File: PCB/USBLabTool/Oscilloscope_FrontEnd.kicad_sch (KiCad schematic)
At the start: 61 parts, among them J1 Chanel 1 input, J10 GPIO, J11 T_buf, J12 T_N5V, J13 ADC, J14 +3.3 V, J2 2174507-2, J3 T_att, J4 Conn_01x01, J5 T_acdc, J6 T_P5V, J7 T_amp, J8 T_pwm, J9 Conn_01x01, K1 G5V-2, Q1 IRLML6402TRPBF, U12 LMP7718, U2 AQY284SX, U3 CD74HC4316M96, U5 LTC1983ES6-5#TRPBF, U6 OPA863

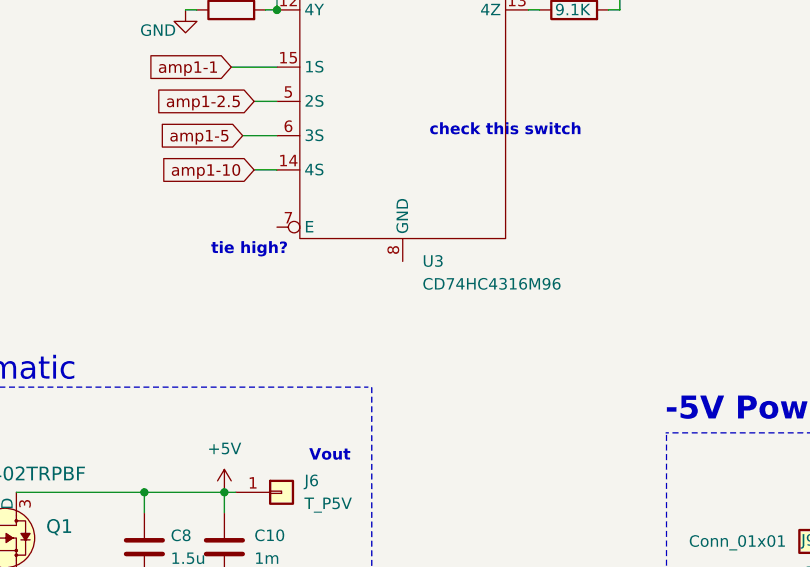
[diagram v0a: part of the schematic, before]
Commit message: added missing GND
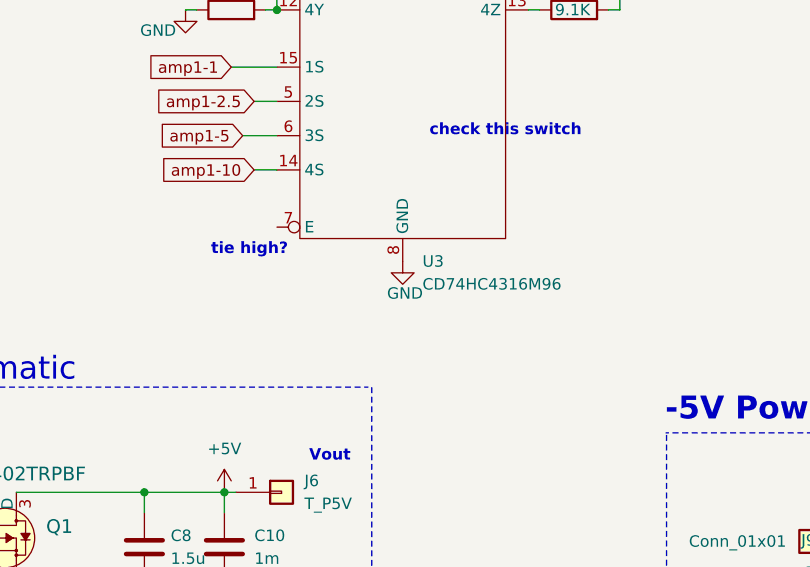
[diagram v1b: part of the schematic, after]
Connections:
- net GND: now also U3.8 (GND)
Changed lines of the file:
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@@
+	)
+	(symbol
+		(lib_id "power:GND")
+		(at 171.45 148.59 0)
+		(unit 1)
+		(exclude_from_sim no)
+		(in_bom yes)
+		(on_board yes)
+		(dnp no)
+		(property "Reference" "#PWR06"
+			(at 171.45 154.94 0)
+			(effects
+				(font
+					(size 1.27 1.27)
+				)
+				(hide yes)
+			)
+		)
+		(property "Value" "GND"
+			(at 171.704 152.146 0)
+			(effects
+				(font
+					(size 1.27 1.27)
+				)
+			)
+		)
+		(property "Footprint" ""
+			(at 171.45 148.59 0)
+			(effects
+				(font
+					(size 1.27 1.27)
+				)
+				(hide yes)
+			)
+		)
+		(property "Datasheet" ""
+			(at 171.45 148.59 0)
+			(effects
+				(font
+					(size 1.27 1.27)
+				)
+				(hide yes)
+			)
+		)
+		(property "Description" ""
+			(at 171.45 148.59 0)
+			(effects
+				(font
+					(size 1.27 1.27)
+				)
+				(hide yes)
+			)
+		)
+		(pin "1"
+		)
+		(instances
+			(project "USBLabTool"
+				(path "/b5440f7d-90d5-417e-adc2-aa6b11e5424d/4269701b-4537-45be-98a2-a1633b405066"
+					(reference "#PWR06")
+					(unit 1)
+				)
+			)
+		)
 	)
 	(symbol

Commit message: Starting PCB layout
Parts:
- removed J10: GPIO, Connector_PinHeader_2.54mm:PinHeader_1x10_P2.54mm_Vertical, symbol Connector_Generic:Conn_01x10
- removed J2: 2174507-2, J_SMD_2174507-2-5_7.8_5_2.71, symbol 2174507-2:2174507-2
- removed Q1: IRLML6402TRPBF, digikey-footprints:SOT-23-3, symbol dk_Transistors-FETs-MOSFETs-Single:IRLML6402TRPBF
- removed U12: LMP7718, Package_SO:VSSOP-8_3x3mm_P0.65mm, symbol USBLabTool:LMP7718MM/NOPB
- removed U3: CD74HC4316M96, symbol USBLabTool:CD74HC4316M96
- removed U5: LTC1983ES6-5#TRPBF, Package_TO_SOT_SMD:SOT-23-6_Handsoldering, symbol LTC1983ES6-5_TRPBF:LTC1983ES6-5#TRPBF
- added C11, C12, C16, C24, C26, c23: 100n, Capacitor_SMD:C_0603_1608Metric_Pad1.08x0.95mm_HandSolder, symbol Device:C
- added C11: 47n, Capacitor_SMD:C_0603_1608Metric_Pad1.08x0.95mm_HandSolder, symbol Device:C
- added C25: 160p, Capacitor_SMD:C_0603_1608Metric_Pad1.08x0.95mm_HandSolder, symbol Device:C
- added C5: 200p, Capacitor_SMD:C_0603_1608Metric_Pad1.08x0.95mm_HandSolder, symbol Device:C
- added D3: 1N4148, Diode_THT:D_DO-35_SOD27_P7.62mm_Horizontal, symbol Diode:1N4148
- added D4: BAV199DW, Package_TO_SOT_SMD:SOT-23, symbol Diode:BAV199DW
- added GD2: GDT_SH90, footprints:GDT_SH_LTF, symbol Device:GDT_2Pin
- added J10: T_pwm, Connector_PinHeader_2.54mm:PinHeader_1x01_P2.54mm_Vertical, symbol Connector_Generic:Conn_01x01
- added J15: ADC2, Connector_PinHeader_2.54mm:PinHeader_1x01_P2.54mm_Vertical, symbol Connector_Generic:Conn_01x01
- added J16: +3.3 V, Connector_PinHeader_2.54mm:PinHeader_1x01_P2.54mm_Vertical, symbol Connector_Generic:Conn_01x01
- added J2: Chanel 1 input, Connector_PinHeader_2.54mm:PinHeader_1x01_P2.54mm_Vertical, symbol Connector_Generic:Conn_01x01
- added K2: G5V-2, Relay_THT:Relay_DPDT_Omron_G5V-2, symbol Relay:G5V-2
- added L2: 10u, Inductor_SMD:L_0603_1608Metric_Pad1.05x0.95mm_HandSolder, symbol pspice:INDUCTOR
- added R18: 68K, Resistor_SMD:R_0603_1608Metric_Pad0.98x0.95mm_HandSolder, symbol Device:R
- added R19: 820K, Resistor_SMD:R_0603_1608Metric_Pad0.98x0.95mm_HandSolder, symbol Device:R
- added R20: 200k, Resistor_SMD:R_0603_1608Metric_Pad0.98x0.95mm_HandSolder, symbol Device:R
- added R21: 240, Resistor_SMD:R_0603_1608Metric_Pad0.98x0.95mm_HandSolder, symbol Device:R
- added R22, R27, R31: 1K, Resistor_SMD:R_0603_1608Metric_Pad0.98x0.95mm_HandSolder, symbol Device:R
- added R23, R28: 6.2, Resistor_SMD:R_0603_1608Metric_Pad0.98x0.95mm_HandSolder, symbol Device:R
- added R24: 1.5K, Resistor_SMD:R_0603_1608Metric_Pad0.98x0.95mm_HandSolder, symbol Device:R
- added R25: 3.9K, Resistor_SMD:R_0603_1608Metric_Pad0.98x0.95mm_HandSolder, symbol Device:R
- added R26: 9.1K, Resistor_SMD:R_0603_1608Metric_Pad0.98x0.95mm_HandSolder, symbol Device:R
- added R29, R30: 2K, Resistor_SMD:R_0603_1608Metric_Pad0.98x0.95mm_HandSolder, symbol Device:R
- added R32: 100, Resistor_SMD:R_0603_1608Metric_Pad0.98x0.95mm_HandSolder, symbol Device:R
- added U1: AQY284SX, Package_SO:SOP-4_3.8x4.1mm_P2.54mm, symbol Relay_SolidState:TLP3123
- added U3 (x2): CD74HC4316M96, Package_SO:SOIC-16_3.9x9.9mm_P1.27mm, symbol USBLabTool:CD74HC4316M96
- added U5, U8: LMP7718, Package_SO:VSSOP-8_3x3mm_P0.65mm, symbol USBLabTool:LMP7718MM/NOPB
- added U7: OPA863, Package_TO_SOT_SMD:SOT-23-6_Handsoldering, symbol Amplifier_Operational:ADA4807-1
- C10: value 1m -> 820p
- C14: value 10u -> 100n
- C15: value 1u -> 100n
- C20: value 10u -> 1u
- C6: value 10u -> 820p
- C8: value 1.5u -> 68p
- GD2: renamed from GD1; footprint digikey-footprints:SH90_1 -> footprints:GDT_SH_LTF
- J12: value T_N5V -> T_buf
- J14: renamed from J13; value ADC -> ADC1
- J4: value Conn_01x01 -> T_att
- J6: value T_P5V -> T_acdc
- J9: value Conn_01x01 -> T_amp
- R6: value 27k -> 820K
- renumbered C7 to C10, C17 to C16, C9 to C17, C12 to C18, C13 to C20, C21 to C26, C22 to C28, C1 to C5, C2 to C6, C3 to C7, C4 to C8, D1 to D2, D2 to D4, J8 to J10, J11 to J12, J14 to J16, J3 to J4, J7 to J8, R5 to R10, R7 to R12, R9 to R17, R11 to R18, R10 to R19, R12 to R20, R13 to R23, R15 to R27, R14 to R29, R16 to R30, R17 to R32, R1 to R5, R2 to R6, R3 to R7, R4 to R8
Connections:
- net +3.3V: now also C26.1, D4.1 (A1), J16.1 (Pin_1)
- net +5V: now also C15.1, C16.1, U3.16 (V_CC), U3.16 (V_CC), U5.8 (V+), U7.5 (~{DISABLE}), U7.6 (V+), U8.8 (V+), c23.2; no longer C10.1, C14.1, C8.2, J6.1 (Pin_1), J9.1 (Pin_1)
- net -5V: now also C14.1, C11.1, C12.1, C24.1, U3.9 (V_EE), U3.9 (V_EE), U5.4 (V-), U7.2 (V-), U8.4 (V-); no longer C20.1, J12.1 (Pin_1)
- net GND: now also C15.2, C11.2, C12.2, C16.2, C24.2, C25.2, C26.2, C5.1, D3.2 (A), D4.2 (K2), GD2.2, K2.1, R18.1, R19.1, R22.1, R29.2, U1.2, U3.7 (E), U3.7 (E), U3.8 (GND), U3.8 (GND), c23.1; no longer C6.2, R6.2
- net acdc: now also R21.2
- net amp1-1: now also U3.15 (1S)
- net amp1-10: now also U3.14 (4S)
- net amp1-2.5: now also U3.5 (2S)
- net amp1-5: now also U3.6 (3S)
- net attenuate: now also D3.1 (K), K2.16
- net at C10.2, J5.1 (Pin_1), U2.3: now also U8.3 (+IN_A)
- net at C6.1: now also C5.2, K2.6, R19.2, R20.1; no longer J4.1 (Pin_1)
- net at J8.1 (Pin_1), R17.2, R18.2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: now also U8.1 (OUT_A)
- net at R17.1: now also U3.1 (1Z)
- net at R27.1, R30.1: now also U8.6 (-IN_B)
- net at R20.1: now also U3.13 (4Z)
- net at R23.2, R29.2: now also U8.5 (+IN_B)
- net at R12.2: now also U3.11 (3Y), U3.12 (4Y), U3.2 (1Y), U3.3 (2Y), U8.2 (-IN_A)
- net at R30.2, U6.3 (+): now also U8.7 (OUT_B)
- net at R6.1: now also C10.1, C8.2, K2.8, R18.2; no longer C8.1
- net at R19.1: now also U3.10 (3Z)
- net at R18.1: now also U3.4 (2Z)
- net ADC renamed ADC1
- net pwm renamed TIM2_CH1
- new net: C8.1, K2.9, R6.2
- new net: R23.1, U3.1 (1Z)
- new net: J9.1 (Pin_1), R23.2, R24.2, R25.2, R26.2, R27.1, U5.1 (OUT_A)
- new net: R25.1, U3.10 (3Z)
- new net: R29.1, R31.1, U5.6 (-IN_B)
- new net: R31.2, U5.7 (OUT_B), U7.3 (+)
- new net: J12.1 (Pin_1), R32.1, U7.1, U7.4 (-)
- new net: C20.1, J10.1 (Pin_1), L2.2, R30.1
- new net: R27.2, R30.2, U5.5 (+IN_B)
- new net: R24.1, U3.4 (2Z)
- new net: R22.2, U3.11 (3Y), U3.12 (4Y), U3.2 (1Y), U3.3 (2Y), U5.2 (-IN_A)
- new net: C6.2, K2.11, R20.2
- new net: C11.2, J6.1 (Pin_1), U1.3, U5.3 (+IN_A)
- new net: R21.1, U1.1
- new net: C11.1, J4.1 (Pin_1), K2.4, U1.4
- new net: GD2.1, J2.1 (Pin_1), K2.13
- new net: R26.1, U3.13 (4Z)
- new net: L2.1, R28.2
- new net ADC2: C25.1, D4.3 (K3A4), J15.1 (Pin_1), R32.2
- new net TIM2_CH2: R28.1
- new net amp2-1: U3.15 (1S)
- new net amp2-10: U3.14 (4S)
- new net amp2-2.5: U3.5 (2S)
- new net amp2-5: U3.6 (3S)
- no-connect marks 3 -> 0
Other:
- note added: "SCOPE CHAN 0"
- note added: "SCOPE CHAN 1"
- note added: "it's active low for the switch so ground the E"
- note removed: "-5V Power supply"
- note removed: "USB Soft Start Schematic"
- note removed: "Vout"
- note removed: "move these things to the Power_Supply sheet -5V might not be needed (awg already has it?) usb plug should be with MCU probably (psu part on power supply)"
- note removed: "need to change this to actual mcu pins"
- moved on the sheet: C10, C16, C17, C18, C20, C26, C28, C5, C6, C7, C8, D2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

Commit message: Finished PCB traces
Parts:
- J1: value Chanel 1 input -> Chanel 0 input
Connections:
- net acdc renamed CH0 ACDC
- net CH0 ACDC: no longer R21.2
- net attenuate renamed CH0_attenuate
- net CH0_attenuate: no longer D3.1 (K), K2.16
- new net CH1 ACDC: R21.2
- new net CH1_attenuate: D3.1 (K), K2.16
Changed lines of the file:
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@@
 		)
 	)
-	(text "tie high?"
-		(exclude_from_sim no)
-		(at 143.256 240.03 0)
-		(effects
-			(font
-				(size 1.27 1.27)
-				(thickness 0.254)
-				(bold yes)
-			)
-		)
-	)
 	(text "check this switch"
 		(exclude_from_sim no)
@@
 		)
 	)
-	(global_label "attenuate"
+	(global_label "CH1_attenuate"
 		(shape input)
 		(at 46.99 180.34 180)
@@
 		)
 		(property "Intersheetrefs" "${INTERSHEET_REFS}"
-			(at 35.6264 180.2606 0)
+			(at 30.2769 180.34 0)
 			(effects
 				(font
@@
 		)
 	)
-	(global_label "acdc"
+	(global_label "CH0 ACDC"
 		(shape input)
 		(at 119.38 73.66 180)
@@
 		)
 		(property "Intersheetrefs" "${INTERSHEET_REFS}"
-			(at 112.4917 73.5806 0)
+			(at 106.7186 73.66 0)
 			(effects
 				(font
@@
 		)
 	)
-	(global_label "acdc"
+	(global_label "CH1 ACDC"
 		(shape input)
 		(at 110.49 185.42 180)
@@
 		)
 		(property "Intersheetrefs" "${INTERSHEET_REFS}"
-			(at 103.6017 185.3406 0)
+			(at 97.8286 185.42 0)
 			(effects
 				(font
@@
 		)
 	)
-	(global_label "attenuate"
+	(global_label "CH0_attenuate"
 		(shape input)
 		(at 55.88 68.58 180)
@@
 		)
 		(property "Intersheetrefs" "${INTERSHEET_REFS}"
-			(at 44.5164 68.5006 0)
+			(at 39.1669 68.58 0)
 			(effects
 				(font
@@
 			)
 		)
-		(property "Value" "Chanel 1 input"
+		(property "Value" "Chanel 0 input"
 			(at 27.178 86.106 90)
 			(effects

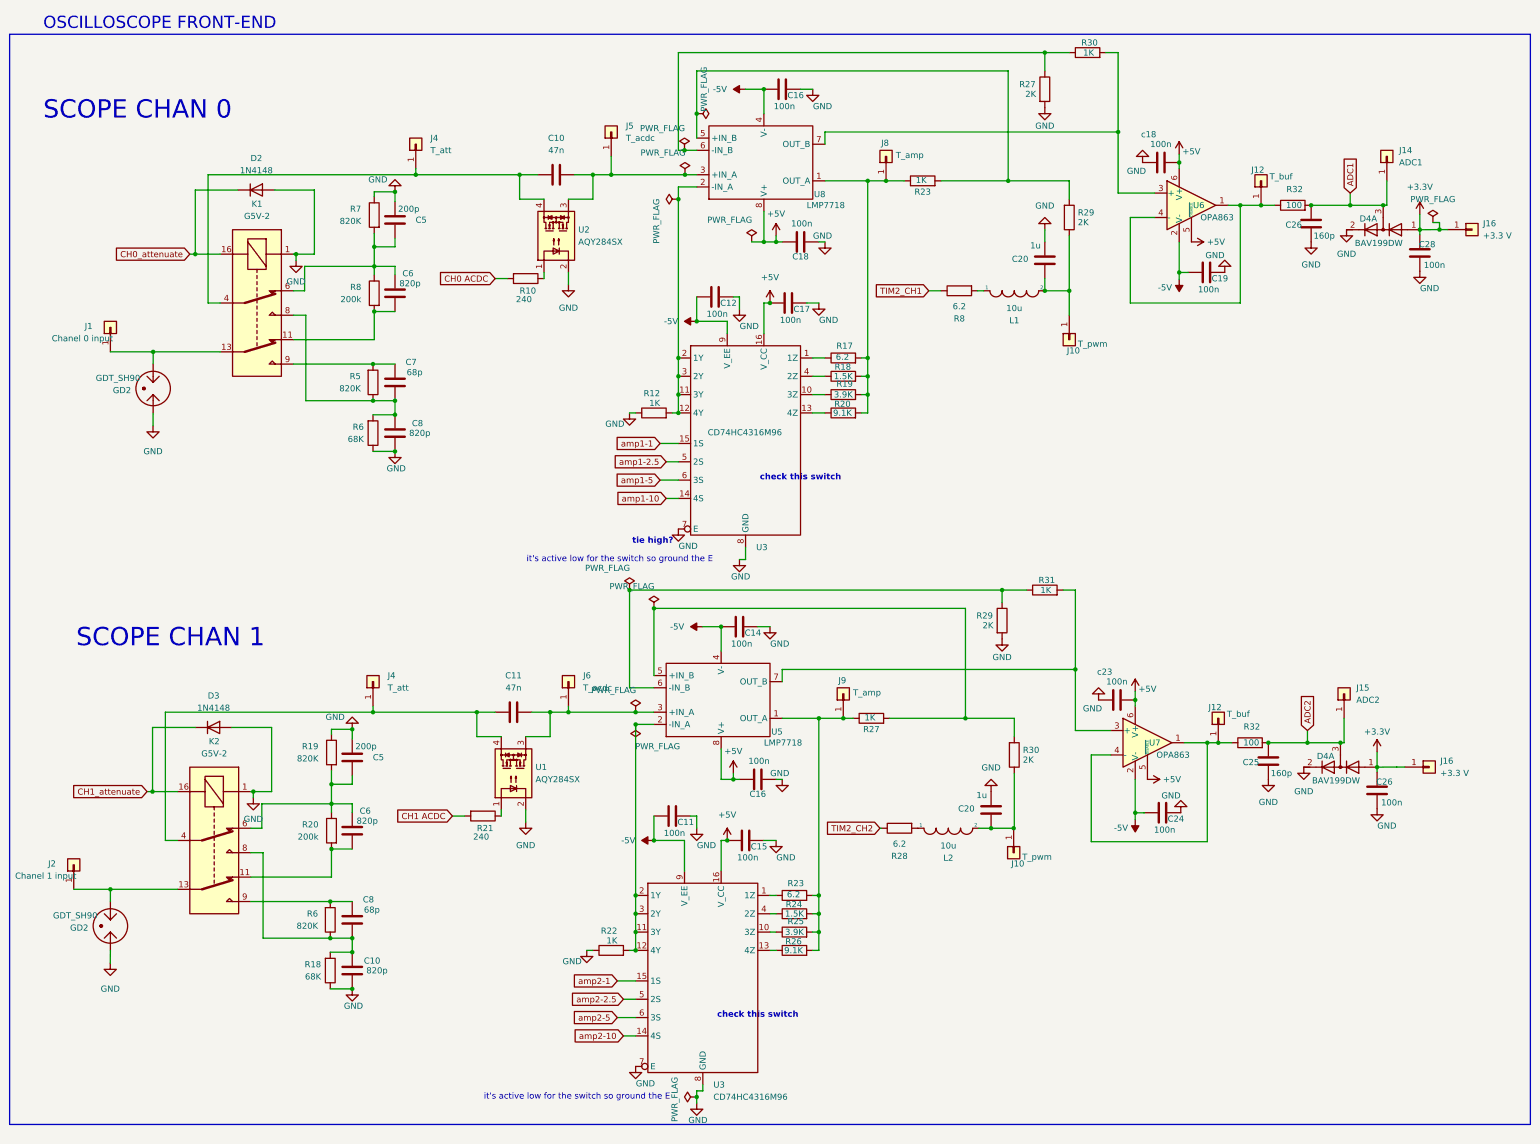
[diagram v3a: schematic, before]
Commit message: Moving files to where they should be
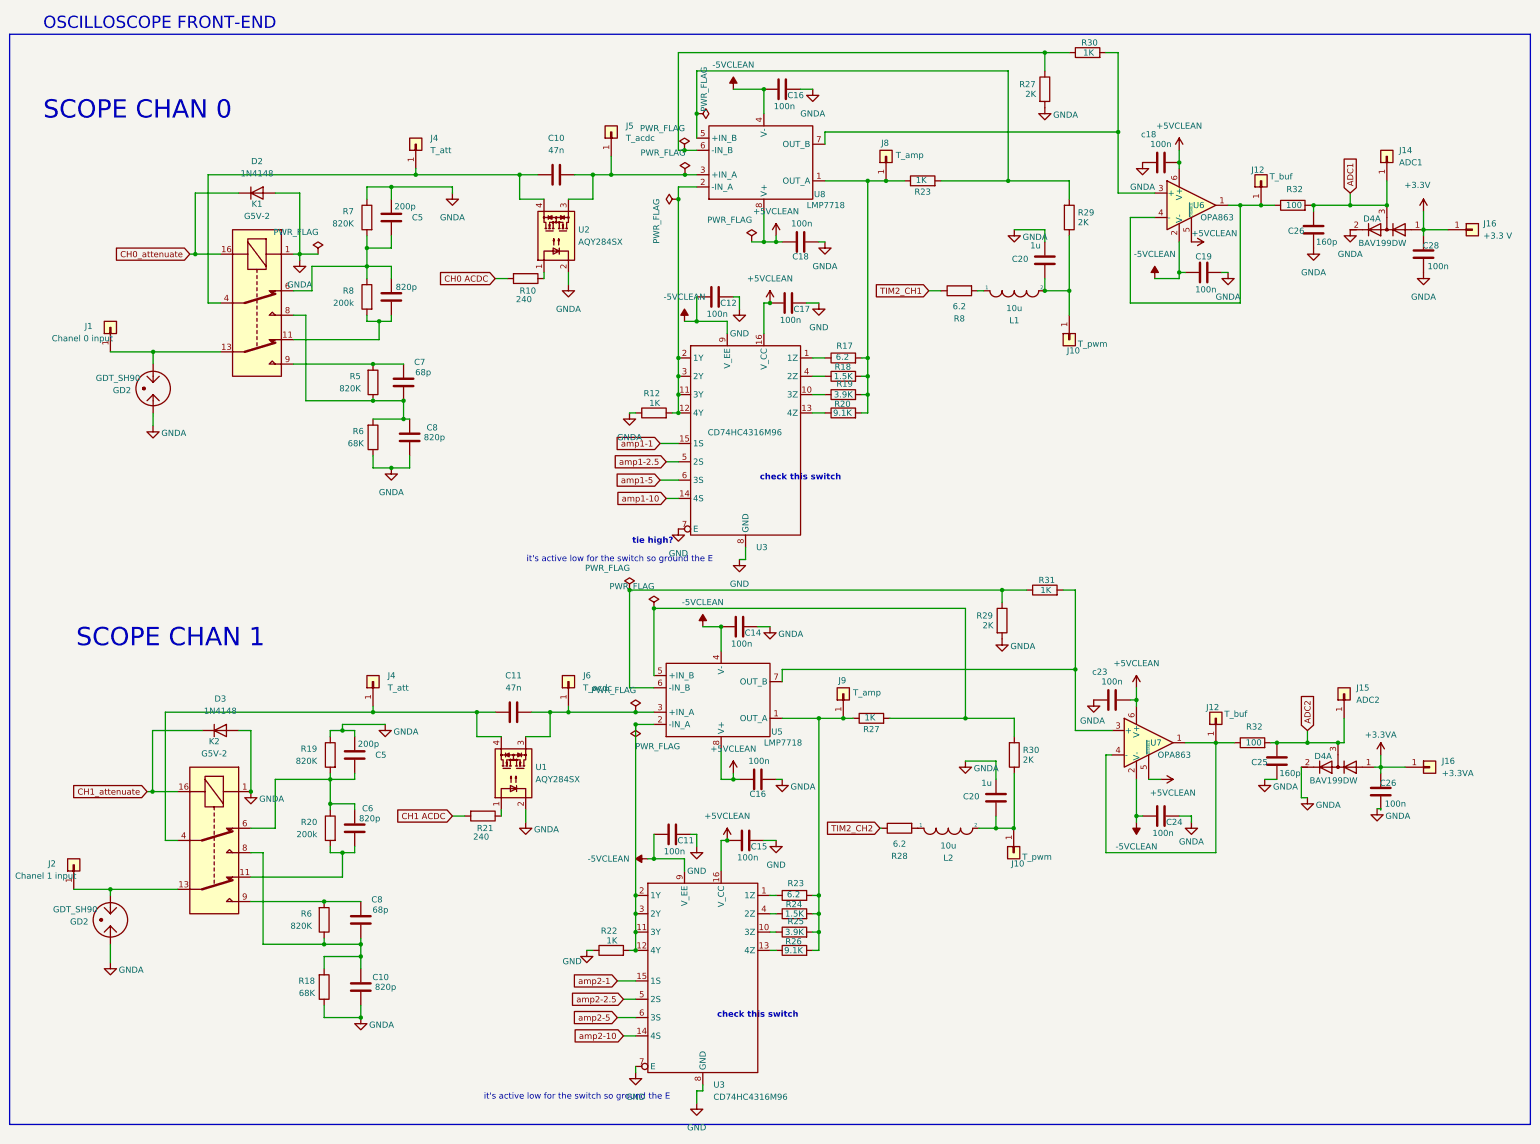
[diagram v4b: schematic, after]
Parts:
- J16: value +3.3 V -> +3.3VA
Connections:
- net +3.3V: no longer C26.1, D4.1 (A1), J16.1 (Pin_1)
- net GND: no longer C10.2, C14.2, C16.2, C16.2, C18.2, C19.2, C20.2, C20.2, C24.2, C25.2, C26.2, C26.2, C28.2, C5.1, C5.1, C8.2, D2.2 (A), D3.2 (A), D4.2 (K2), D4.2 (K2), GD2.2, GD2.2, K1.1, K2.1, R12.1, R18.1, R19.1, R27.2, R29.2, R6.1, R7.1, U1.2, U2.2, c18.1, c23.1
- net +5V renamed +5VCLEAN
- net -5V renamed -5VCLEAN
- new net +3.3VA: C26.1, D4.1 (A1), J16.1 (Pin_1)
- new net GNDA: C10.2, C14.2, C16.2, C16.2, C18.2, C19.2, C20.2, C20.2, C24.2, C25.2, C26.2, C26.2, C28.2, C5.1, C5.1, C8.2, D2.2 (A), D3.2 (A), D4.2 (K2), D4.2 (K2), GD2.2, GD2.2, K1.1, K2.1, R12.1, R18.1, R19.1, R27.2, R29.2, R6.1, R7.1, U1.2, U2.2, c18.1, c23.1
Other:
- moved on the sheet: C10, C11, C19, C20, C24, C25, C26, C28, C5, C6, C7, C8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

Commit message: Moving files to where they should be
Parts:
- D4: footprint Package_TO_SOT_SMD:SOT-23 -> Package_TO_SOT_SMD:SOT-363_SC-70-6_Handsoldering
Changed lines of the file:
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@@
 			)
 		)
-		(property "Footprint" "Package_TO_SOT_SMD:SOT-23"
+		(property "Footprint" "Package_TO_SOT_SMD:SOT-363_SC-70-6_Handsoldering"
 			(at 292.1 63.5 0)
 			(effects
@@
 			)
 		)
+		(property "Purpose" ""
+			(at 304.8 63.5 0)
+			(effects
+				(font
+					(size 1.27 1.27)
+				)
+				(hide yes)
+			)
+		)
 		(pin "1"
 		)
@@
 			)
 		)
-		(property "Footprint" "Package_TO_SOT_SMD:SOT-23"
+		(property "Footprint" "Package_TO_SOT_SMD:SOT-363_SC-70-6_Handsoldering"
 			(at 281.94 175.26 0)
 			(effects
@@
 			(at 294.64 175.26 0)
 			(effects
+				(font
+					(size 1.27 1.27)
+				)
+				(hide yes)
+			)
+		)
+		(property "Purpose" ""
+			(at 294.64 175.26 0)
+			(effects

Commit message: Update Oscilloscope_FrontEnd.kicad_sch
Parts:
- J16: value +3.3 V -> +3.3VA
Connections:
- net +3.3V is gone; now on net +3.3VA: C28.1, D4.1 (A1), J16.1 (Pin_1)
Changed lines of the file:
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@@
 			)
 		)
-		(property "Value" "+3.3V"
+		(property "Value" "+3.3VA"
 			(at 311.15 54.229 0)
 			(effects
@@
 		(fields_autoplaced yes)
 		(property "Reference" "J16"
-			(at 324.866 62.2299 0)
+			(at 325.12 62.2299 0)
 			(effects
 				(font
@@
 			)
 		)
-		(property "Value" "+3.3 V"
-			(at 324.866 64.7699 0)
+		(property "Value" "+3.3VA"
+			(at 325.12 64.7699 0)
 			(effects
 				(font
